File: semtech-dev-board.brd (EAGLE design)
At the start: 160 x 100 mm, 58 parts, among them Q1 BSS123, U1 SEMTECH_SX1236, U3 MIC5219 3.3V, X1 BU-SMA-G, X2 BU-SMA-G, X3 BU-SMA-G, X4 BU-SMA-G

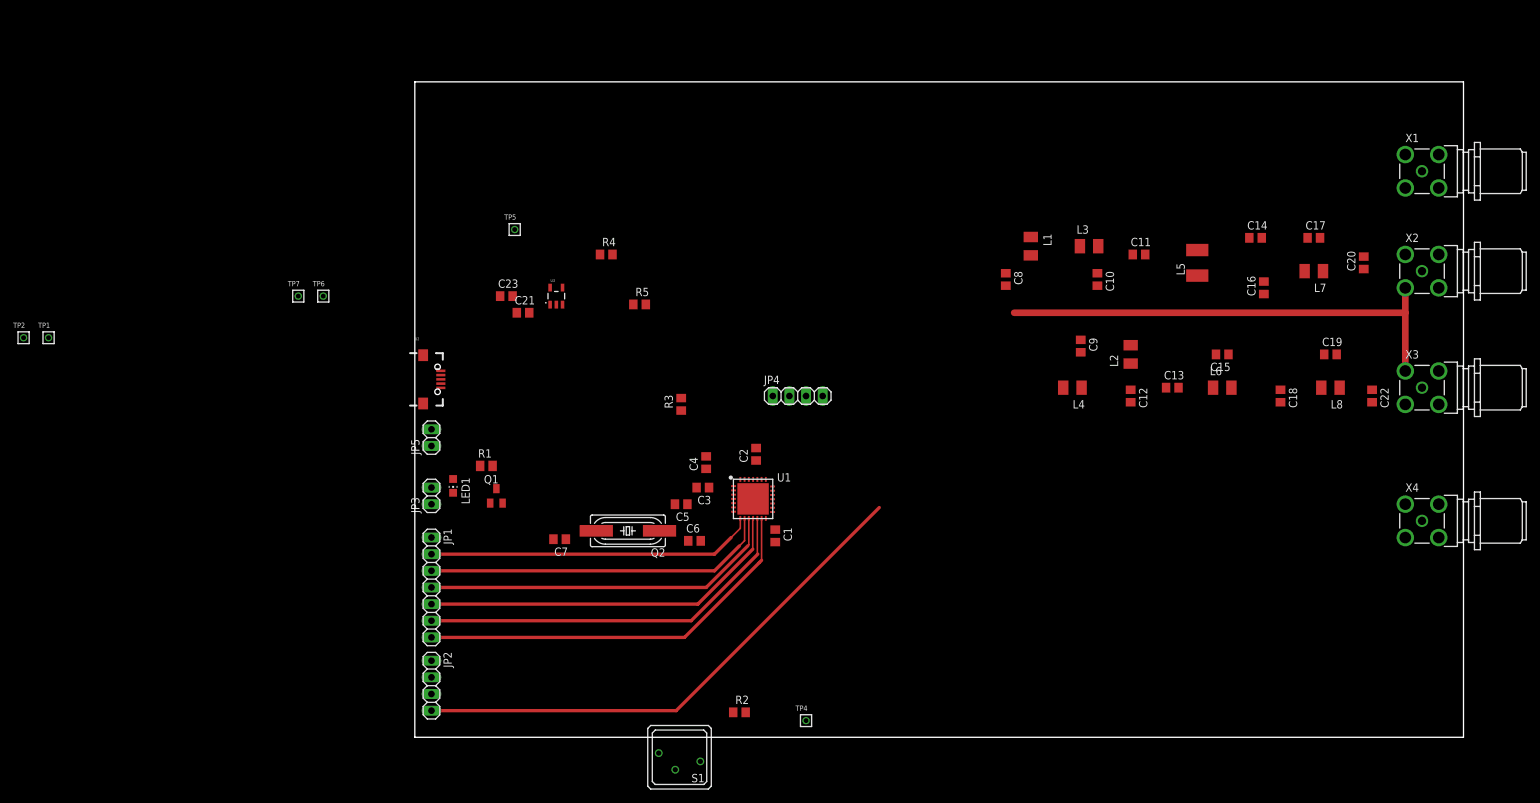
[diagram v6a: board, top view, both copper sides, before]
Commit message: Draft arrangement of components
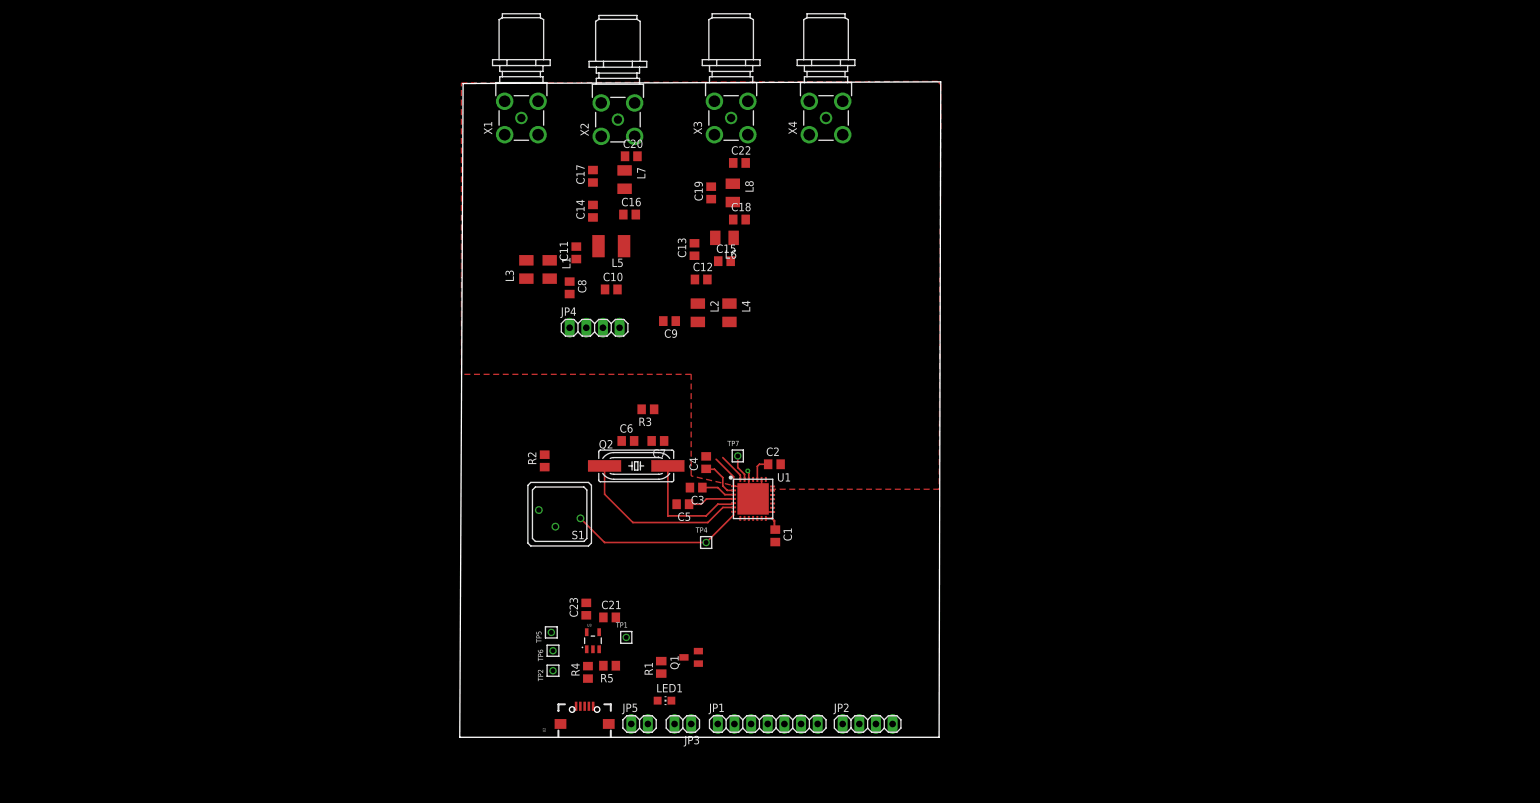
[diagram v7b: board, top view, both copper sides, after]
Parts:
- moved X1 137.7 mm to (16.3, 94.5), turned to 90 degrees
- moved X2 124.8 mm to (31.0, 94.2), turned to 90 degrees
- moved X3 113.2 mm to (48.3, 94.5), turned to 90 degrees
- moved C20 112.9 mm to (33.0, 88.6), turned to 0 degrees
- moved C17 110.4 mm to (27.2, 85.6), turned to 90 degrees
- moved X4 109.8 mm to (62.7, 94.5), turned to 90 degrees
- moved L7 106.1 mm to (32.0, 85.1), turned to 270 degrees
- moved C22 102.9 mm to (49.5, 87.6), turned to 0 degrees
- moved C14 101.2 mm to (27.2, 80.3), turned to 90 degrees
- moved TP1 99.3 mm to (32.3, 15.2)
- moved C19 97.6 mm to (45.2, 83.1), turned to 90 degrees
- moved C16 97.4 mm to (32.8, 79.8), turned to 0 degrees
- moved L8 95.9 mm to (48.5, 83.1), turned to 270 degrees
- moved TP2 95.4 mm to (21.1, 10.2), turned to 90 degrees
- moved L5 89.4 mm to (30.0, 74.9), turned to 180 degrees
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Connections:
- net N$3 renamed SPI_MOSI
- net N$4 renamed SPI_MISO
- net N$5 renamed SPI_SCK
- removed net AGND: C10.2, C12.2, C16.2, C18.2, C20.2, C22.2, C4.2, C5.2, C8.2, C9.2, U1.0, U1.15, U1.23, U1.26, X1.2, X1.3, X1.4, X1.5, X2.2, X2.3, X2.4, X2.5, X3.2, X3.3, X3.4, X3.5, X4.2, X4.3, X4.4, X4.5
- net GND: now also C10.2, C12.2, C16.2, C18.2, C20.2, C22.2, C4.2, C5.2, C8.2, C9.2, U1.0, U1.15, U1.23, U1.26, X1.2, X1.3, X1.4, X1.5, X2.2, X2.3, X2.4, X2.5, X3.2, X3.3, X3.4, X3.5, X4.2, X4.3, X4.4, X4.5
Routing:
- net SPI_NSS: track 81.2 -> 0.00 mm
- net AGND: track 72.4 -> 0.00 mm
- net DIO5: track 61.6 -> 0.00 mm
- net DIO4: track 59.5 -> 0.00 mm
- net DIO3: track 57.2 -> 0.00 mm
- net DIO2: track 55.1 -> 0.00 mm
- net DIO1: track 53.1 -> 0.00 mm
- net DIO0: track 50.3 -> 0.00 mm
- net SX1236_RST: track 0.00 -> 27.1 mm
- net XTALB: track 0.00 -> 26.7 mm
- net N$2: track 0.00 -> 18.4 mm
- net GND: track 0.00 -> 12.0 mm, vias 0 -> 1
- net VBAT: track 0.00 -> 11.8 mm
- net VR_DIG: track 0.00 -> 7.13 mm
- net VR_ANA: track 0.00 -> 6.29 mm
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- added copper zone on layer 1, net GND
- removed copper zone on layer 2, net AGND
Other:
- board size 160 x 100 mm -> 73.4 x 100 mm

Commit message: board draft
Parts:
- moved L3 28.4 mm to (39.3, 53.7)
- moved C8 25.9 mm to (43.6, 52.1), turned to 0 degrees
- moved JP4 24.2 mm to (46.5, 47.5)
- moved L1 23.2 mm to (40.6, 59.7), turned to 0 degrees
- moved S1 22.2 mm to (39.4, 20.1)
- moved R2 21.5 mm to (31.5, 24.1), turned to 180 degrees
- moved C7 18.3 mm to (22.6, 34.0)
- moved C6 18.0 mm to (22.9, 30.0), turned to 180 degrees
- moved C11 15.3 mm to (39.1, 68.8)
- moved C9 15.3 mm to (49.0, 52.1)
- moved C19 13.9 mm to (58.9, 80.5)
- moved C14 13.9 mm to (39.1, 73.2)
- moved L4 13.3 mm to (53.3, 52.6)
- moved C13 12.5 mm to (53.2, 67.7)
- moved L6 12.2 mm to (58.9, 72.6), turned to 270 degrees
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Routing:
- net SX1236_RST: track 27.1 -> 5.34 mm
- net XTALB: track 26.7 -> 17.8 mm
- net N$2: track 18.4 -> 22.9 mm
- net PA_BOOST: track 4.01 -> 0.00 mm
- net VBAT: track 11.8 -> 15.6 mm
- net GND: track 12.0 -> 10.6 mm, vias 1 -> 0
- net VR_DIG: track 7.13 -> 6.32 mm
- net VR_ANA: track 6.29 -> 7.03 mm
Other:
- board size 73.4 x 100 mm -> 58.1 x 96.4 mm
